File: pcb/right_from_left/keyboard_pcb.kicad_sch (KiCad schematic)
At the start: 44 parts, among them J1 TRRS, J2 Conn_01x04_Male, K0 KEYSW, K1 KEYSW, K10 KEYSW, K11 KEYSW, K12 KEYSW, K13 KEYSW, K14 KEYSW, K15 KEYSW, K2 KEYSW, K20 KEYSW, K21 KEYSW, K22 KEYSW, K23 KEYSW, K24 KEYSW, K25 KEYSW, K3 KEYSW, K30 KEYSW, K31 KEYSW, K32 KEYSW, K4 KEYSW, K5 KEYSW, U1 PCF8574, U2 Pico

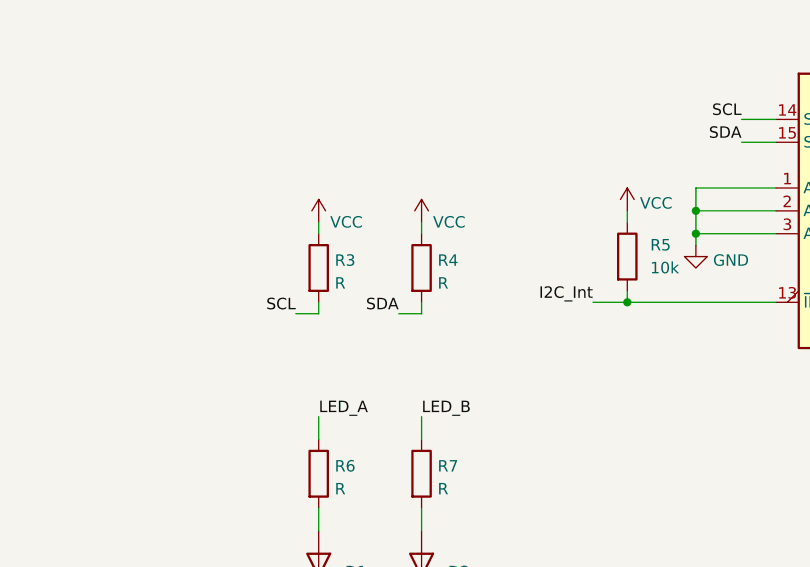
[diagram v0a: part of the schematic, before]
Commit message: right_from_left is ready for review
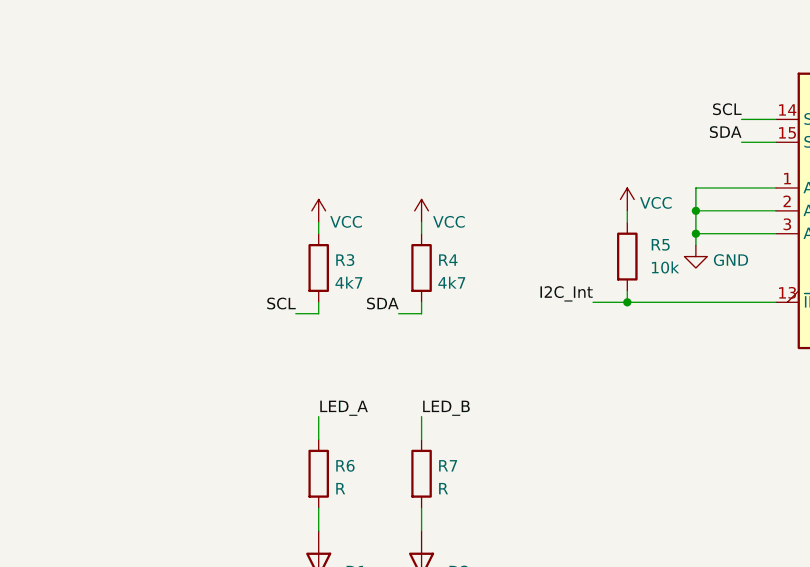
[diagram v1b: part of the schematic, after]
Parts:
- R3, R4: value R -> 4k7
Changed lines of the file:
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@@
       (effects (font (size 1.27 1.27)) (justify left))
     )
-    (property "Value" "R" (at 164.338 147.7522 0)
+    (property "Value" "4k7" (at 164.338 147.7522 0)
       (effects (font (size 1.27 1.27)) (justify left))
     )
@@
       (effects (font (size 1.27 1.27)) (justify left))
     )
-    (property "Value" "R" (at 152.908 147.7522 0)
-      (effects (font (size 1.27 1.27)) (justify left))
-    )
+    (property "Value" "4k7" (at 152.908 147.7522 0)
+      (effects (font (size 1.27 1.27)) (justify left))
+    )

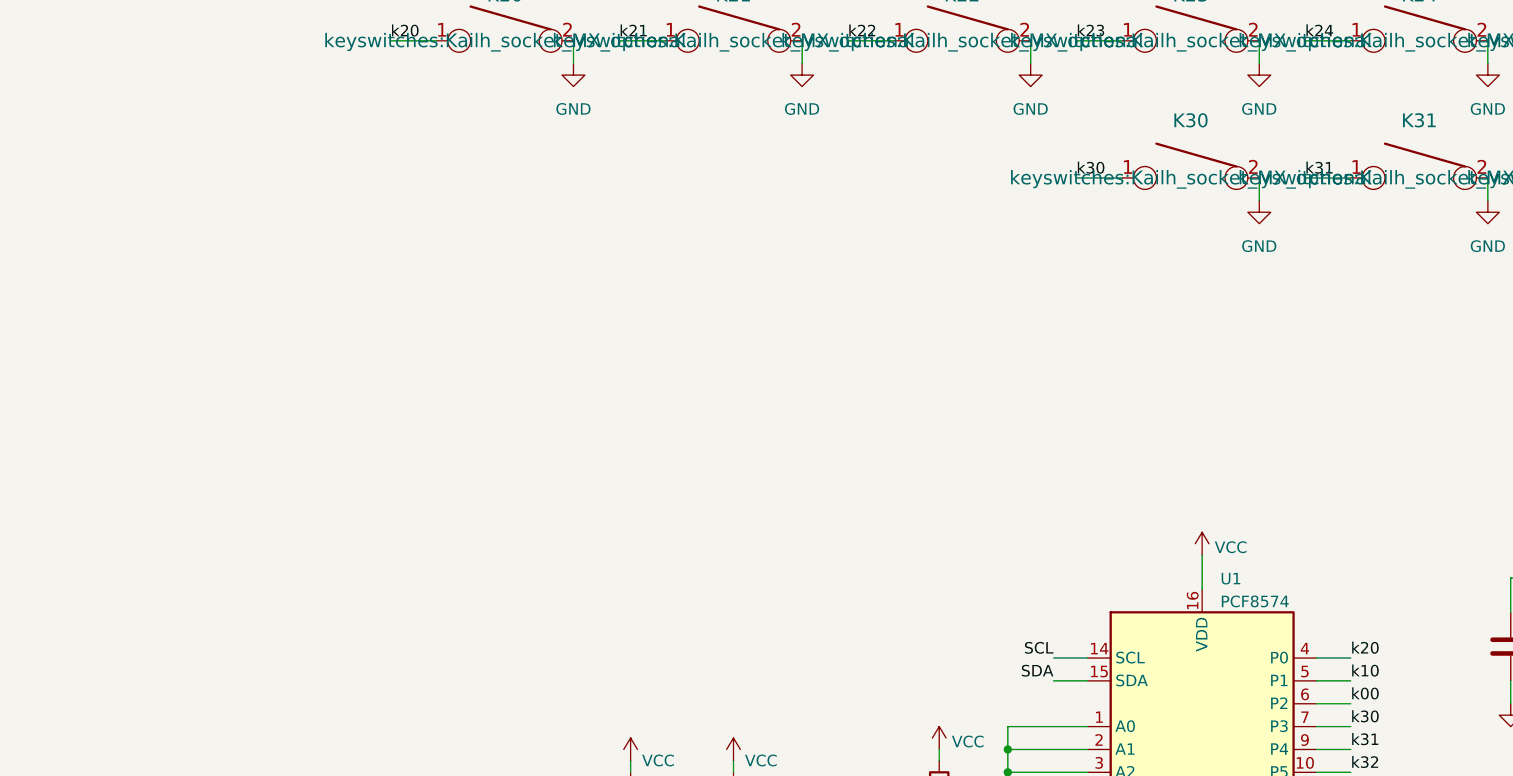
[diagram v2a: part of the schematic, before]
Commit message: left keyboards routed
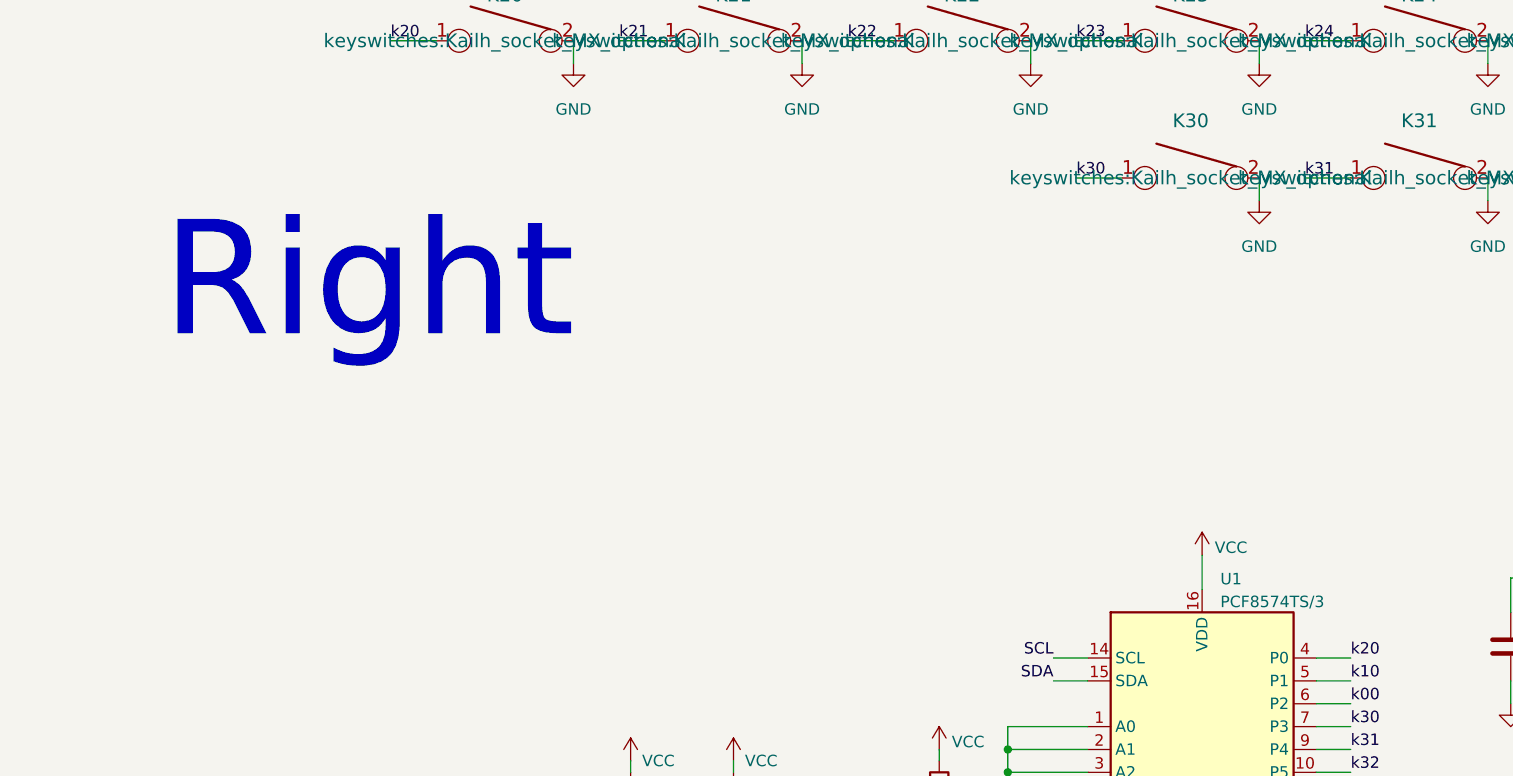
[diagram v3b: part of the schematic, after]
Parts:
- R3, R4: footprint Resistor_SMD:R_0603_1608Metric_Pad0.98x0.95mm_HandSolder -> Resistor_SMD:R_0805_2012Metric
- U1: value PCF8574 -> PCF8574TS/3
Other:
- note added: "Right"
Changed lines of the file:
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@@
     (effects (font (size 1.27 1.27)) (justify left bottom))
+  )
+  (text "Right" (at 99.06 95.25 0)
+    (effects (font (face "KiCad Font") (size 12.7 12.7)) (justify left bottom))
   )
   (label "k11" (at 72.39 74.93 0) (fields_autoplaced)
@@
       (effects (font (size 1.27 1.27)) (justify left))
     )
-    (property "Footprint" "Resistor_SMD:R_0603_1608Metric_Pad0.98x0.95mm_HandSolder" (at 160.782 146.05 90)
+    (property "Footprint" "Resistor_SMD:R_0805_2012Metric" (at 160.782 146.05 90)
       (effects (font (size 1.27 1.27)) hide)
     )
@@
       (effects (font (size 1.27 1.27)) (justify left))
     )
-    (property "Value" "PCF8574" (at 216.6494 123.2971 0)
+    (property "Value" "PCF8574TS/3" (at 216.6494 123.2971 0)
       (effects (font (size 1.27 1.27)) (justify left))
     )
@@
       (effects (font (size 1.27 1.27)) (justify left))
     )
-    (property "Footprint" "Resistor_SMD:R_0603_1608Metric_Pad0.98x0.95mm_HandSolder" (at 149.352 146.05 90)
-      (effects (font (size 1.27 1.27)) hide)
-    )
+    (property "Footprint" "Resistor_SMD:R_0805_2012Metric" (at 149.352 146.05 90)
+      (effects (font (size 1.27 1.27)) hide)
+    )

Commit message: Revision 1.1 WIP#
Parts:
- removed C1: 10uF, Capacitor_SMD:C_0603_1608Metric_Pad1.08x0.95mm_HandSolder, symbol Device:C
- removed C2: 100nF, Capacitor_SMD:C_0603_1608Metric_Pad1.08x0.95mm_HandSolder, symbol Device:C
- removed J2: Conn_01x04_Male, Connector_PinHeader_2.54mm:PinHeader_1x04_P2.54mm_Vertical, symbol Connector:Conn_01x04_Male
- removed MB1, MB2, MB3, MB4: MountingHole, beekeeb_lib:mousebites, symbol Mechanical:MountingHole
- removed U1: PCF8574TS/3, Package_SO:SSOP-20_4.4x6.5mm_P0.65mm, symbol Interface_Expansion:PCF8574
- added C3: 10uF, Capacitor_SMD:C_0603_1608Metric_Pad1.08x0.95mm_HandSolder, symbol Device:C
- added C4: 100nF, Capacitor_SMD:C_0603_1608Metric_Pad1.08x0.95mm_HandSolder, symbol Device:C
- added H5, H6, H7, H8: MountingHole, beekeeb_lib:MountingHole_2.2mm_M2-8mm, symbol Mechanical:MountingHole
- added R10, R11, R12, R13, R14, R8, R9: 10k, Resistor_SMD:R_0603_1608Metric_Pad0.98x0.95mm_HandSolder, symbol Device:R
- added TP1: TestPoint, TestPoint:TestPoint_Pad_D3.0mm, symbol Connector:TestPoint
- added U3: PCF8574TS, Package_SO:SSOP-20_4.4x6.5mm_P0.65mm, symbol Interface_Expansion:PCF8574TS
- added U4: MCP23009-E/SO, Package_SO:SOIC-18W_7.5x11.6mm_P1.27mm, symbol mcp23009:MCP23009-E/SO
- K0, K1, K10, K11, K12, K13, K14, K15, K2, K20, K21, K22, K23, K24, K25, K3, K30, K31, K32, K4, K5: footprint keyswitches:Kailh_socket_MX_optional_platemount -> keyswitches:Kailh_socket_MX_optional_platemount_3d_pretty_by_datasheet
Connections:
- net GND: now also C3.2, C4.2, U3.15 (VSS), U3.6 (A0), U3.7 (A1), U3.9 (A2), U4.18 (VSS), U4.5 (ADR)
- net I2C_Int: now also U3.1 (~{INT}), U4.7 (INT)
- net LED_A: now also U3.19 (P6), U4.14 (GP6)
- net LED_B: now also U3.20 (P7), U4.15 (GP7)
- net SCL: now also U3.2 (SCL), U4.3 (SCL)
- net SDA: now also U3.4 (SDA), U4.4 (SDA)
- net VBUS: now also J1.2 (TIP)
- net k00: now also R8.1, U3.12 (P2), U4.10 (GP2)
- net k04: now also U2.7 (GPIO5); no longer U2.36 (3V3)
- net k05: now also U2.6 (GPIO4); no longer U2.37 (3V3_EN)
- net k10: now also R9.1, U3.11 (P1), U4.9 (GP1)
- net k20: now also R10.1, U3.10 (P0), U4.8 (GP0)
- net k30: now also R11.1, U3.14 (P3), U4.11 (GP3)
- net k31: now also R12.1, U3.16 (P4), U4.12 (GP4)
- net k32: now also R13.1, U3.17 (P5), U4.13 (GP5)
- net rx: now also U2.1 (GPIO0); no longer U2.2 (GPIO1)
- net tx: now also U2.2 (GPIO1); no longer U2.1 (GPIO0)
- net VCC renamed +3.3V
- net +3.3V: now also U2.36 (3V3), C3.1, C4.1, R10.2, R11.2, R12.2, R13.2, R14.1, R8.2, R9.2, U3.5 (VDD), U4.1 (VDD); no longer J1.2 (TIP), U2.39 (VSYS)
- new net MCP_RST: R14.2, TP1.1, U4.6 (~{RESET})
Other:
- note added: "I2C 1"
- moved on the sheet: D1, D2, H1, H2, H3, H4, J1, R1, R2, R3, R4, R6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

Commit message: Rev 1.1 WIP
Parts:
- removed R5: 10k, Resistor_SMD:R_0603_1608Metric_Pad0.98x0.95mm_HandSolder, symbol Device:R
- removed U3: PCF8574TS, Package_SO:SSOP-20_4.4x6.5mm_P0.65mm, symbol Interface_Expansion:PCF8574TS
- R3, R4: footprint Resistor_SMD:R_0805_2012Metric -> Resistor_SMD:R_0603_1608Metric
- U2: footprint RPi_Pico:RPi_Pico_SMD_TH -> misc:RPi_Pico_SMD_TH
- renumbered U4 to U1

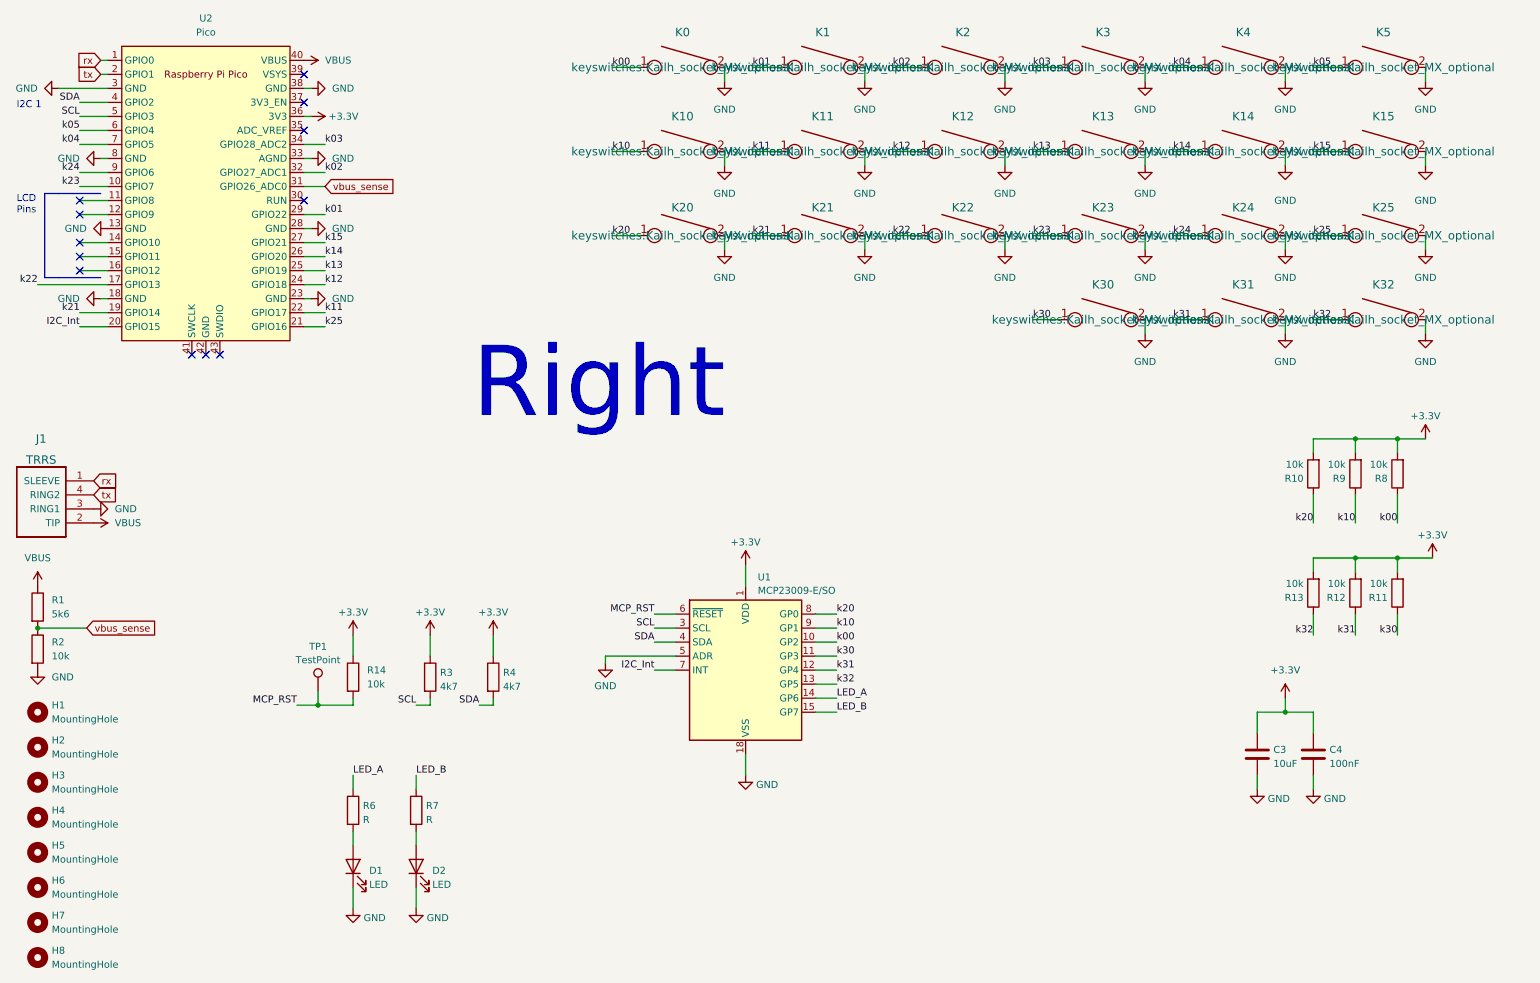
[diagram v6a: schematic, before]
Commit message: Revision 1.1 -RFR- new standoff holes added and left/right pcb positions synced
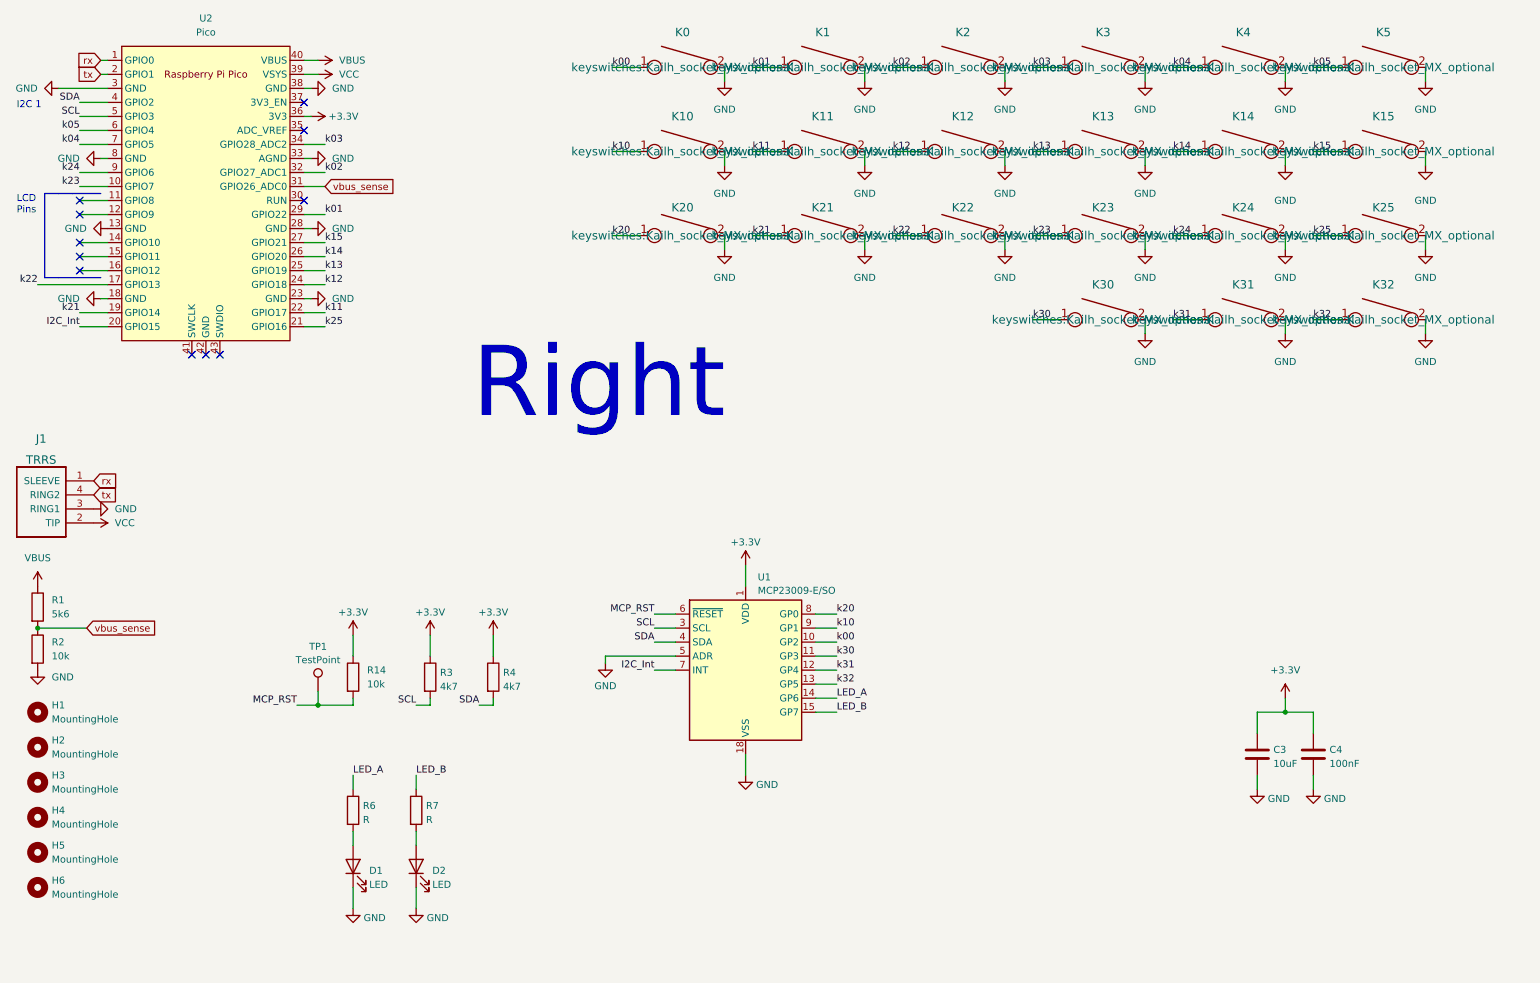
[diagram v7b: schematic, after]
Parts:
- removed H7, H8: MountingHole, beekeeb_lib:MountingHole_2.2mm_M2-8mm, symbol Mechanical:MountingHole
- removed R10, R11, R12, R13, R8, R9: 10k, Resistor_SMD:R_0603_1608Metric_Pad0.98x0.95mm_HandSolder, symbol Device:R
- H1, H2, H3, H4, H5, H6: footprint beekeeb_lib:MountingHole_2.2mm_M2-8mm -> misc:MountingHole_3.7mm_Pad_TopBottom
- R1, R14, R2, R6, R7: footprint Resistor_SMD:R_0603_1608Metric_Pad0.98x0.95mm_HandSolder -> Resistor_SMD:R_0603_1608Metric
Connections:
- net VBUS: no longer J1.2 (TIP)
- net VCC: now reaches U2.39 (VSYS)
- net VCC: now also J1.2 (TIP)
- no-connect marks 12 -> 11
